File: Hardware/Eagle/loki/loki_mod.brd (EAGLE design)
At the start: 21.9 x 22.9 mm, 38 parts

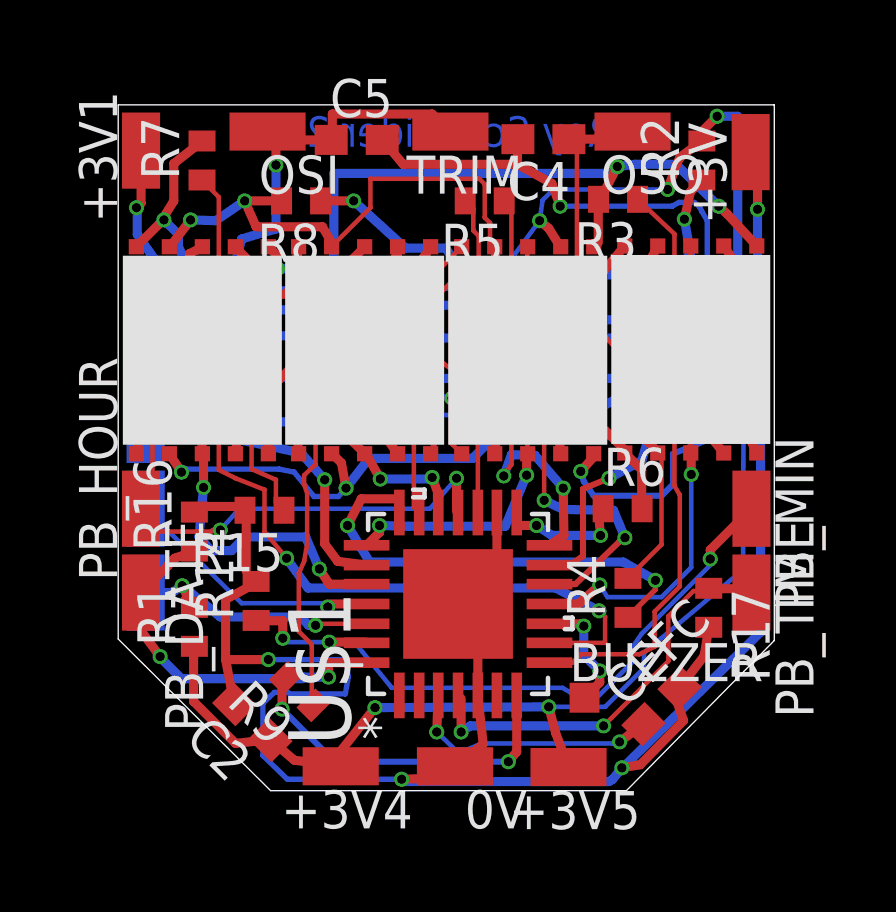
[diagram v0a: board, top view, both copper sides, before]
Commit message: After feedback from the manufacturer of the PCB the outer PCB shape has been improved.
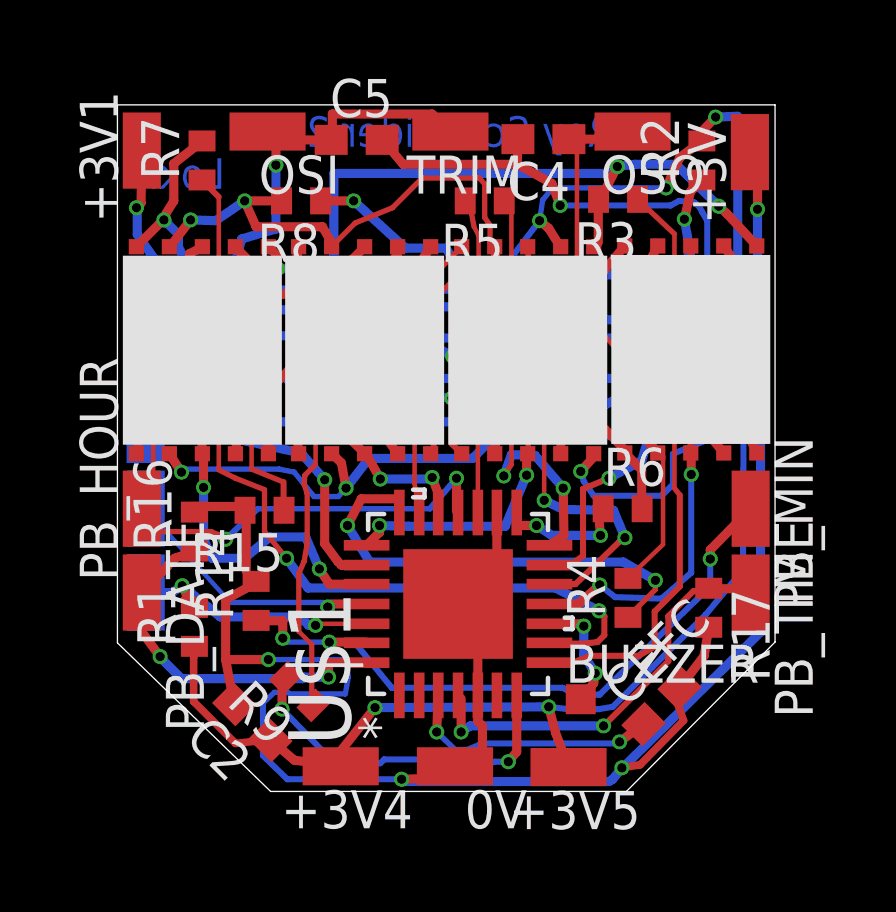
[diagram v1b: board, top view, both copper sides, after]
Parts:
- moved BUZZER 0.14 mm to (15.4, 2.92)
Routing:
- net N$3: track 24.5 -> 23.8 mm
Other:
- outline, holes or cut-outs redrawn
- board text added: "Loki"

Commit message: Fixed some DRC issues.
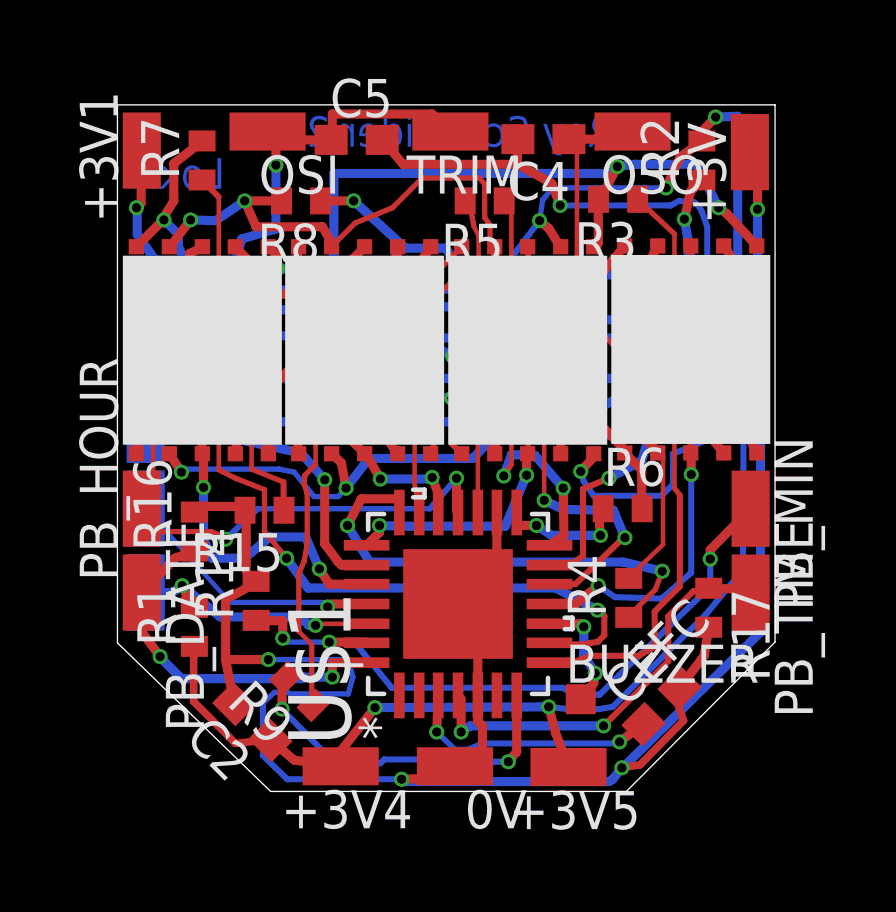
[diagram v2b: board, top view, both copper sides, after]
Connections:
- removed net RA2/SW4: U$1.1

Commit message: Added resitor for piezo.
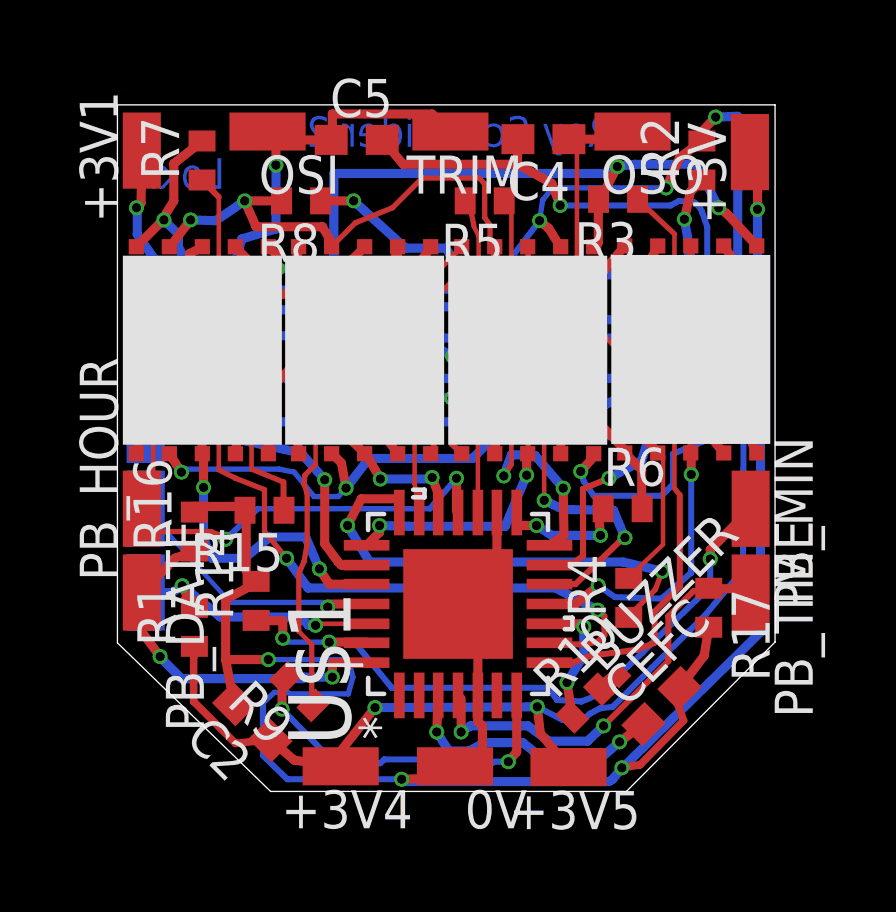
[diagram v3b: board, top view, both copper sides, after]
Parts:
- added R10: 820, resistor:R0402
- BUZZER: value TPSQTP10SQ -> TPTP06SQ; device testpad:TP10SQ -> testpad:TP06SQ
- moved BUZZER 1.49 mm to (16.7, 3.71), turned to 45 degrees
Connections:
- new net N$1: BUZZER.TP, R10.2
- net PIEZO: now also R10.1; no longer BUZZER.TP
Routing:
- net N$1: track 0.00 -> 0.78 mm
- net VDDCORE/VCAP: track 8.59 -> 9.17 mm
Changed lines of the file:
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@@
 <element name="1M" library="l104g" package="L104G" value="L104G" x="16.5862" y="11.43"/>
 <element name="R9" library="resistor" package="R0402" value="105" x="6.0452" y="3.175" rot="R135"/>
-<element name="BUZZER" library="testpad" package="TP10SQ" value="TPSQTP10SQ" x="15.4178" y="2.921">
-<attribute name="TP_SIGNAL_NAME" value="" x="15.4178" y="2.921" size="1.778" layer="27" display="off"/>
+<element name="R10" library="resistor" package="R0402" value="820" x="15.5956" y="2.794" rot="R45"/>
+<element name="BUZZER" library="testpad" package="TP06SQ" value="TPTP06SQ" x="16.6878" y="3.7084" rot="R45">
+<attribute name="TP_SIGNAL_NAME" value="" x="16.6878" y="3.7084" size="1.778" layer="27" rot="R45" display="off"/>
 </element>
 </elements>
@@
 <via x="19.7358" y="7.5946" extent="1-16" drill="0.3048"/>
 <wire x1="17.4752" y1="4.4704" x2="17.0942" y2="4.1148" width="0.2032" layer="16"/>
-<wire x1="17.0942" y1="4.1148" x2="16.0528" y2="3.0734" width="0.2032" layer="16"/>
-<wire x1="16.0528" y1="3.0734" x2="15.24" y2="3.0734" width="0.2032" layer="16"/>
-<wire x1="15.24" y1="3.0734" x2="14.8082" y2="3.302" width="0.2032" layer="16"/>
-<wire x1="14.8082" y1="3.302" x2="9.1186" y2="3.302" width="0.2032" layer="16"/>
+<wire x1="17.0942" y1="4.1148" x2="16.002" y2="3.0734" width="0.2032" layer="16"/>
+<wire x1="14.3256" y1="3.302" x2="9.1186" y2="3.302" width="0.2032" layer="16"/>
 <wire x1="9.1186" y1="3.302" x2="7.874" y2="4.826" width="0.2032" layer="16"/>
 <wire x1="17.4752" y1="4.4704" x2="18.0086" y2="5.0038" width="0.2032" layer="16"/>
 <wire x1="18.0086" y1="5.0038" x2="19.7358" y2="6.6802" width="0.2032" layer="16"/>
 <wire x1="19.7358" y1="6.6802" x2="19.7358" y2="7.5946" width="0.2032" layer="16"/>
+<wire x1="16.002" y1="3.0734" x2="15.4432" y2="2.8448" width="0.2032" layer="16"/>
+<wire x1="15.4432" y1="2.8448" x2="14.6304" y2="2.8956" width="0.2032" layer="16"/>
+<wire x1="14.6304" y1="2.8956" x2="14.3256" y2="3.302" width="0.2032" layer="16"/>
 </signal>
 <signal name="RB0/SW2">
@@
 <wire x1="5.1308" y1="1.524" x2="5.8674" y2="0.889" width="0.3048" layer="1"/>
 <wire x1="5.1308" y1="1.524" x2="5.071440625" y2="1.55795625" width="0.1524" layer="1"/>
-<wire x1="14.5796" y1="1.8034" x2="15.0114" y2="0.6604" width="0.3048" layer="1"/>
-<wire x1="14.351" y1="2.667" x2="14.5796" y2="1.8034" width="0.3048" layer="1"/>
-<wire x1="8.5598" y1="2.6416" x2="14.351" y2="2.667" width="0.3048" layer="16"/>
+<wire x1="14.0716" y1="1.778" x2="15.0114" y2="0.6604" width="0.3048" layer="1"/>
+<wire x1="13.97" y1="2.667" x2="14.0716" y2="1.778" width="0.3048" layer="1"/>
+<wire x1="8.5598" y1="2.6416" x2="13.97" y2="2.667" width="0.3048" layer="16"/>
 <wire x1="7.239" y1="0.9652" x2="8.5598" y2="2.6416" width="0.3048" layer="1"/>
 <wire x1="7.239" y1="0.9652" x2="7.4168" y2="0.6858" width="0.1524" layer="1"/>
@@
 <wire x1="20.828" y1="7.239" x2="19.5834" y2="5.7404" width="0.2032" layer="16"/>
 <wire x1="20.8534" y1="14.9606" x2="20.828" y2="7.239" width="0.2032" layer="16"/>
-<via x="14.351" y="2.667" extent="1-16" drill="0.3048"/>
+<via x="13.97" y="2.667" extent="1-16" drill="0.3048"/>
 <via x="8.5598" y="2.6416" extent="1-16" drill="0.3048"/>
 <via x="11.1506" y="14.351" extent="1-16" drill="0.3048"/>
@@
 <wire x1="5.207" y1="15.0368" x2="4.4704" y2="15.621" width="0.3048" layer="16"/>
 <wire x1="4.4704" y1="15.621" x2="2.286" y2="16.0528" width="0.3048" layer="16"/>
-<wire x1="16.4846" y1="2.667" x2="16.0274" y2="2.5908" width="0.2032" layer="16"/>
-<wire x1="16.0274" y1="2.5908" x2="14.986" y2="2.5908" width="0.2032" layer="16"/>
-<wire x1="14.986" y1="2.5908" x2="14.351" y2="2.667" width="0.2032" layer="16"/>
+<wire x1="16.4846" y1="2.667" x2="16.0528" y2="2.6162" width="0.2032" layer="16"/>
+<wire x1="16.0528" y1="2.6162" x2="15.7226" y2="2.4384" width="0.2032" layer="16"/>
+<wire x1="15.7226" y1="2.4384" x2="15.5448" y2="2.286" width="0.2032" layer="16"/>
+<wire x1="15.5448" y1="2.286" x2="15.367" y2="2.2352" width="0.2032" layer="16"/>
+<wire x1="15.367" y1="2.2352" x2="14.8082" y2="2.2352" width="0.2032" layer="16"/>
+<wire x1="14.8082" y1="2.2352" x2="13.97" y2="2.667" width="0.2032" layer="16"/>
 </signal>
 <signal name="RB2/LED_H2">
@@
 <via x="18.5166" y="14.3256" extent="1-16" drill="0.3048"/>
 <via x="16.8402" y="14.3256" extent="1-16" drill="0.3048"/>
-<wire x1="17.8816" y1="5.842" x2="17.8816" y2="4.6736" width="0.2032" layer="1"/>
-<wire x1="17.8816" y1="4.6736" x2="17.3482" y2="4.3688" width="0.2032" layer="1"/>
+<wire x1="17.8816" y1="5.842" x2="17.8816" y2="4.8006" width="0.2032" layer="1"/>
+<wire x1="17.8816" y1="4.8006" x2="17.2974" y2="4.572" width="0.2032" layer="1"/>
 <wire x1="14.3764" y1="4.1402" x2="15.1384" y2="4.1402" width="0.2032" layer="1"/>
 <wire x1="15.1384" y1="4.1402" x2="15.748" y2="4.3688" width="0.2032" layer="1"/>
-<wire x1="15.748" y1="4.3688" x2="17.3482" y2="4.3688" width="0.2032" layer="1"/>
+<wire x1="15.748" y1="4.3688" x2="17.2974" y2="4.572" width="0.2032" layer="1"/>
 <wire x1="18.542" y1="9.9568" x2="18.7198" y2="9.7282" width="0.1778" layer="1"/>
 <wire x1="18.7198" y1="9.7282" x2="18.7198" y2="6.6802" width="0.2032" layer="1"/>
@@
 <contactref element="CEFC" pad="1"/>
 <wire x1="16.7132" y1="1.4986" x2="17.50915625" y2="2.09135625" width="0.3048" layer="1"/>
-<wire x1="16.4846" y1="1.4478" x2="16.7132" y2="1.4986" width="0.1524" layer="16"/>
-<wire x1="12.1158" y1="1.4478" x2="16.4846" y2="1.4478" width="0.2032" layer="16"/>
-<wire x1="11.6332" y1="1.2446" x2="12.1158" y2="1.4478" width="0.1778" layer="16"/>
-<wire x1="11.2268" y1="1.2446" x2="11.6332" y2="1.2446" width="0.1778" layer="16"/>
-<wire x1="10.6172" y1="1.8288" x2="11.2268" y2="1.2446" width="0.18541875" layer="16"/>
+<wire x1="11.684" y1="1.1938" x2="12.2174" y2="1.4732" width="0.3048" layer="16"/>
+<wire x1="11.0236" y1="1.1938" x2="11.684" y2="1.1938" width="0.3048" layer="16"/>
+<wire x1="10.6172" y1="1.8288" x2="11.0236" y2="1.1938" width="0.3048" layer="16"/>
 <wire x1="10.668" y1="3.048" x2="10.6172" y2="1.8288" width="0.3048" layer="1"/>
 <via x="16.7132" y="1.4986" extent="1-16" drill="0.3048"/>
 <via x="10.6172" y="1.8288" extent="1-16" drill="0.3048"/>
+<wire x1="12.2174" y1="1.4732" x2="13.4874" y2="1.4732" width="0.3048" layer="16"/>
+<wire x1="13.4874" y1="1.4732" x2="14.2494" y2="0.8636" width="0.3048" layer="16"/>
+<wire x1="14.2494" y1="0.8636" x2="15.9766" y2="0.8636" width="0.3048" layer="16"/>
+<wire x1="15.9766" y1="0.8636" x2="16.7132" y2="1.4986" width="0.3048" layer="16"/>
 </signal>
 <signal name="OSC2/RA6">
@@
 <via x="13.0048" y="0.8382" extent="1-16" drill="0.3048"/>
 <wire x1="13.0048" y1="0.8382" x2="12.5476" y2="0.8382" width="0.2032" layer="16"/>
-<wire x1="12.5476" y1="0.8382" x2="12.4206" y2="0.7874" width="0.2032" layer="16"/>
+<wire x1="12.5476" y1="0.8382" x2="12.319" y2="0.7112" width="0.2032" layer="16"/>
 <wire x1="7.2136" y1="0.7874" x2="8.7376" y2="0.7874" width="0.2032" layer="16"/>
 <wire x1="8.7376" y1="0.7874" x2="8.8646" y2="0.9144" width="0.2032" layer="16"/>
 <wire x1="8.8646" y1="0.9144" x2="10.1346" y2="0.9144" width="0.2032" layer="16"/>
-<wire x1="10.1346" y1="0.9144" x2="10.2616" y2="0.7874" width="0.2032" layer="16"/>
-<wire x1="10.2616" y1="0.7874" x2="12.4206" y2="0.7874" width="0.2032" layer="16"/>
+<wire x1="10.1346" y1="0.9144" x2="10.3886" y2="0.7112" width="0.2032" layer="16"/>
+<wire x1="10.3886" y1="0.7112" x2="12.319" y2="0.7112" width="0.2032" layer="16"/>
 </signal>
 <signal name="RA5/SW4">
@@
 <wire x1="11.43" y1="1.8288" x2="11.43" y2="2.9464" width="0.3048" layer="1"/>
 <wire x1="11.7348" y1="2.032" x2="11.43" y2="1.8288" width="0.3048" layer="16"/>
-<wire x1="16.1798" y1="2.032" x2="11.7348" y2="2.032" width="0.3048" layer="16"/>
 <wire x1="18.3388" y1="4.191" x2="16.1798" y2="2.032" width="0.2032" layer="1"/>
 <wire x1="18.3388" y1="5.6896" x2="18.3388" y2="4.191" width="0.2032" layer="1"/>
@@
 <wire x1="19.177" y1="6.5278" x2="19.5938" y2="6.5278" width="0.2032" layer="1"/>
 <wire x1="19.5938" y1="6.5278" x2="19.685" y2="6.619" width="0.1524" layer="1"/>
+<wire x1="11.7348" y1="2.032" x2="13.6652" y2="2.032" width="0.3048" layer="16"/>
+<wire x1="13.6652" y1="2.032" x2="14.351" y2="1.524" width="0.3048" layer="16"/>
+<wire x1="14.351" y1="1.524" x2="15.6464" y2="1.524" width="0.3048" layer="16"/>
+<wire x1="15.6464" y1="1.524" x2="16.1798" y2="2.032" width="0.3048" layer="16"/>
 </signal>
 <signal name="N$4">
@@
 <signal name="PIEZO">
 <contactref element="U$1" pad="10"/>
-<contactref element="BUZZER" pad="TP"/>
 <via x="15.5194" y="5.334" extent="1-16" drill="0.3048"/>
-<wire x1="15.5194" y1="4.3942" x2="15.9004" y2="3.7846" width="0.3048" layer="16"/>
-<via x="15.9004" y="3.7846" extent="1-16" drill="0.3048"/>
-<wire x1="15.9004" y1="3.7846" x2="15.8496" y2="3.4544" width="0.3048" layer="1"/>
-<wire x1="15.8496" y1="3.4544" x2="15.4178" y2="2.921" width="0.3048" layer="1"/>
+<wire x1="15.5194" y1="4.3942" x2="14.9606" y2="3.4798" width="0.3048" layer="16"/>
+<via x="14.9606" y="3.4798" extent="1-16" drill="0.3048"/>
 <wire x1="14.3764" y1="5.4356" x2="15.4432" y2="5.4356" width="0.3048" layer="1"/>
 <wire x1="15.4432" y1="5.4356" x2="15.5194" y2="5.334" width="0.3048" layer="1"/>
 <wire x1="15.5194" y1="5.334" x2="15.5194" y2="4.3942" width="0.3048" layer="16"/>
+<contactref element="R10" pad="1"/>
+<wire x1="15.135978125" y1="2.334378125" x2="14.9606" y2="3.4798" width="0.3048" layer="1"/>
 </signal>
 <signal name="N$6">
@@
 <wire x1="6.2992" y1="8.1026" x2="6.1976" y2="7.5184" width="0.1778" layer="1"/>
 </signal>
+<signal name="N$1">
+<contactref element="BUZZER" pad="TP"/>
+<contactref element="R10" pad="2"/>
+<wire x1="16.05521875" y1="3.25361875" x2="16.6878" y2="3.7084" width="0.508" layer="1"/>
+</signal>
 </signals>

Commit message: Updated resitor values and fine tuned some traces.
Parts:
- CEFC: value 10 uF -> 1 uF
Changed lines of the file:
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@@
 <element name="R1" library="rcl" package="R0402" value="10K" x="2.54" y="5.334" rot="R90"/>
 <element name="C2" library="resistor" package="C0603" value="0.1 uF" x="4.4704" y="2.159" rot="R135"/>
-<element name="CEFC" library="resistor" package="C0603" value="10 uF" x="18.1102" y="2.6924" rot="R45"/>
+<element name="CEFC" library="resistor" package="C0603" value="1 uF" x="18.1102" y="2.6924" rot="R45"/>
 <element name="R2" library="resistor" package="R0402" value="105" x="19.4564" y="20.8788" rot="R90"/>
 <element name="R3" library="resistor" package="R0402" value="105" x="16.6624" y="19.5834" rot="R180"/>
